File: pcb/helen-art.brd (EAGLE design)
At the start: 49.5 x 46 mm, 29 parts, among them IC1 TINY22S, IC2 MCP73811/2

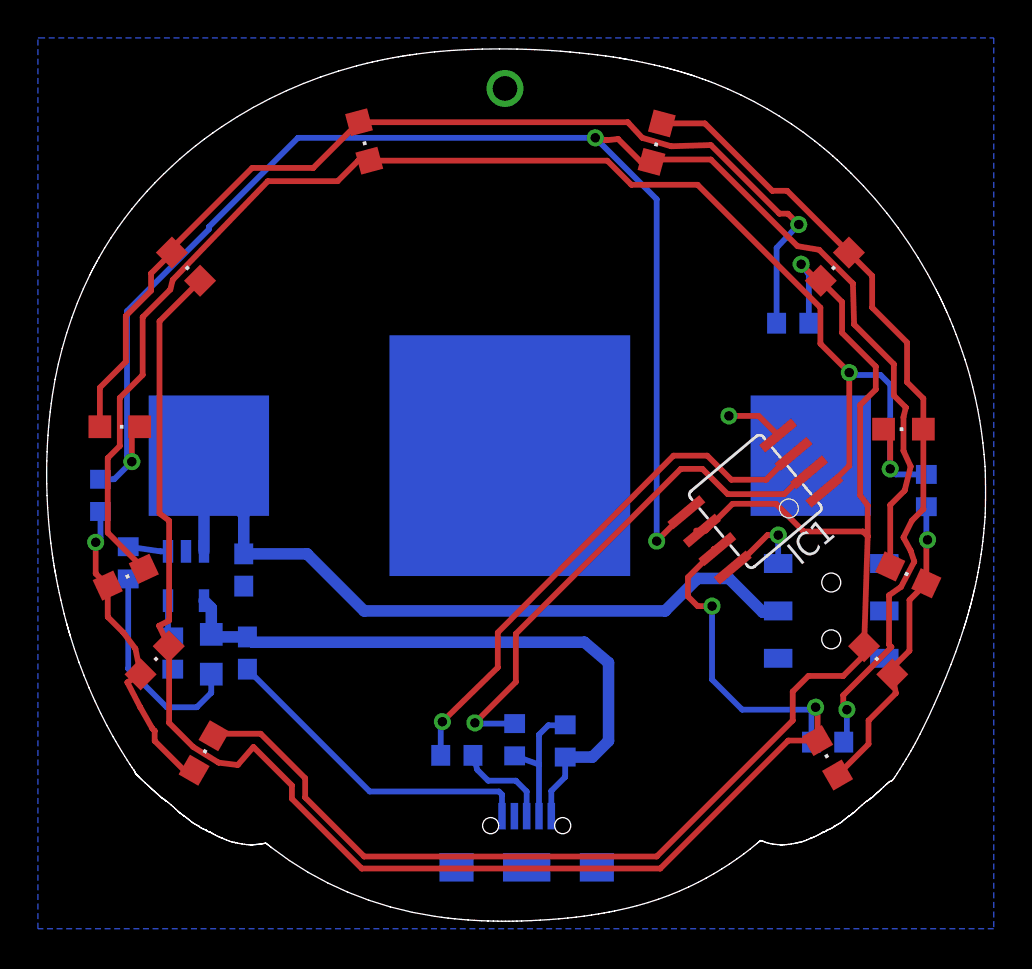
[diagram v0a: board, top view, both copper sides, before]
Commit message: add image back in
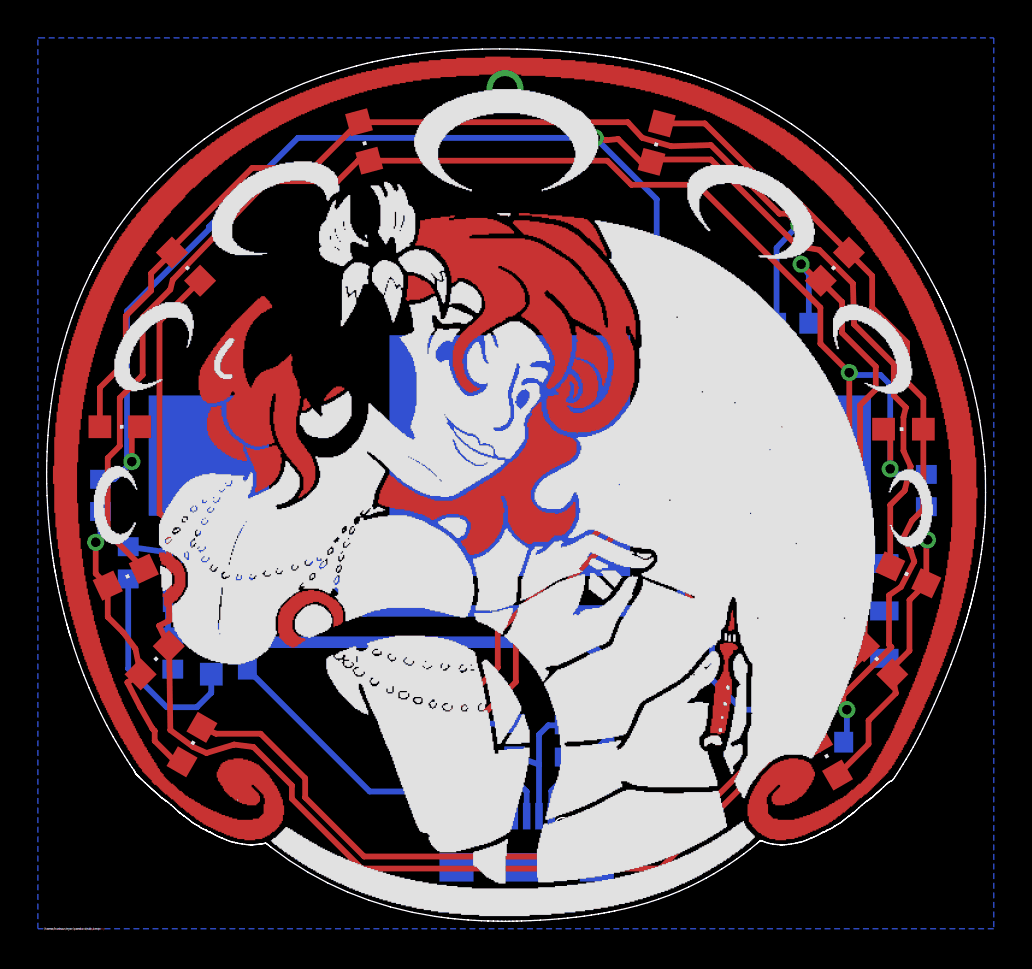
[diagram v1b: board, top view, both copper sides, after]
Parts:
- moved D0 0.78 mm to (7.81, 9.46)
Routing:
- net B1: track 79.6 -> 80.3 mm
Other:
- board text added: "/home/hudson/nycr/pendant/copper.bmp"
- board text added: "/home/hudson/nycr/pendant/mask.bmp"
- board text added: "/home/hudson/nycr/pendant/silk.bmp"
